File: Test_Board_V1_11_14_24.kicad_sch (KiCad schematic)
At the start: 9 parts, among them IC1 FE1.1S, J1 USB-A1HSW6, J2 USB-A1HSW6, J3 USB-A1HSW6

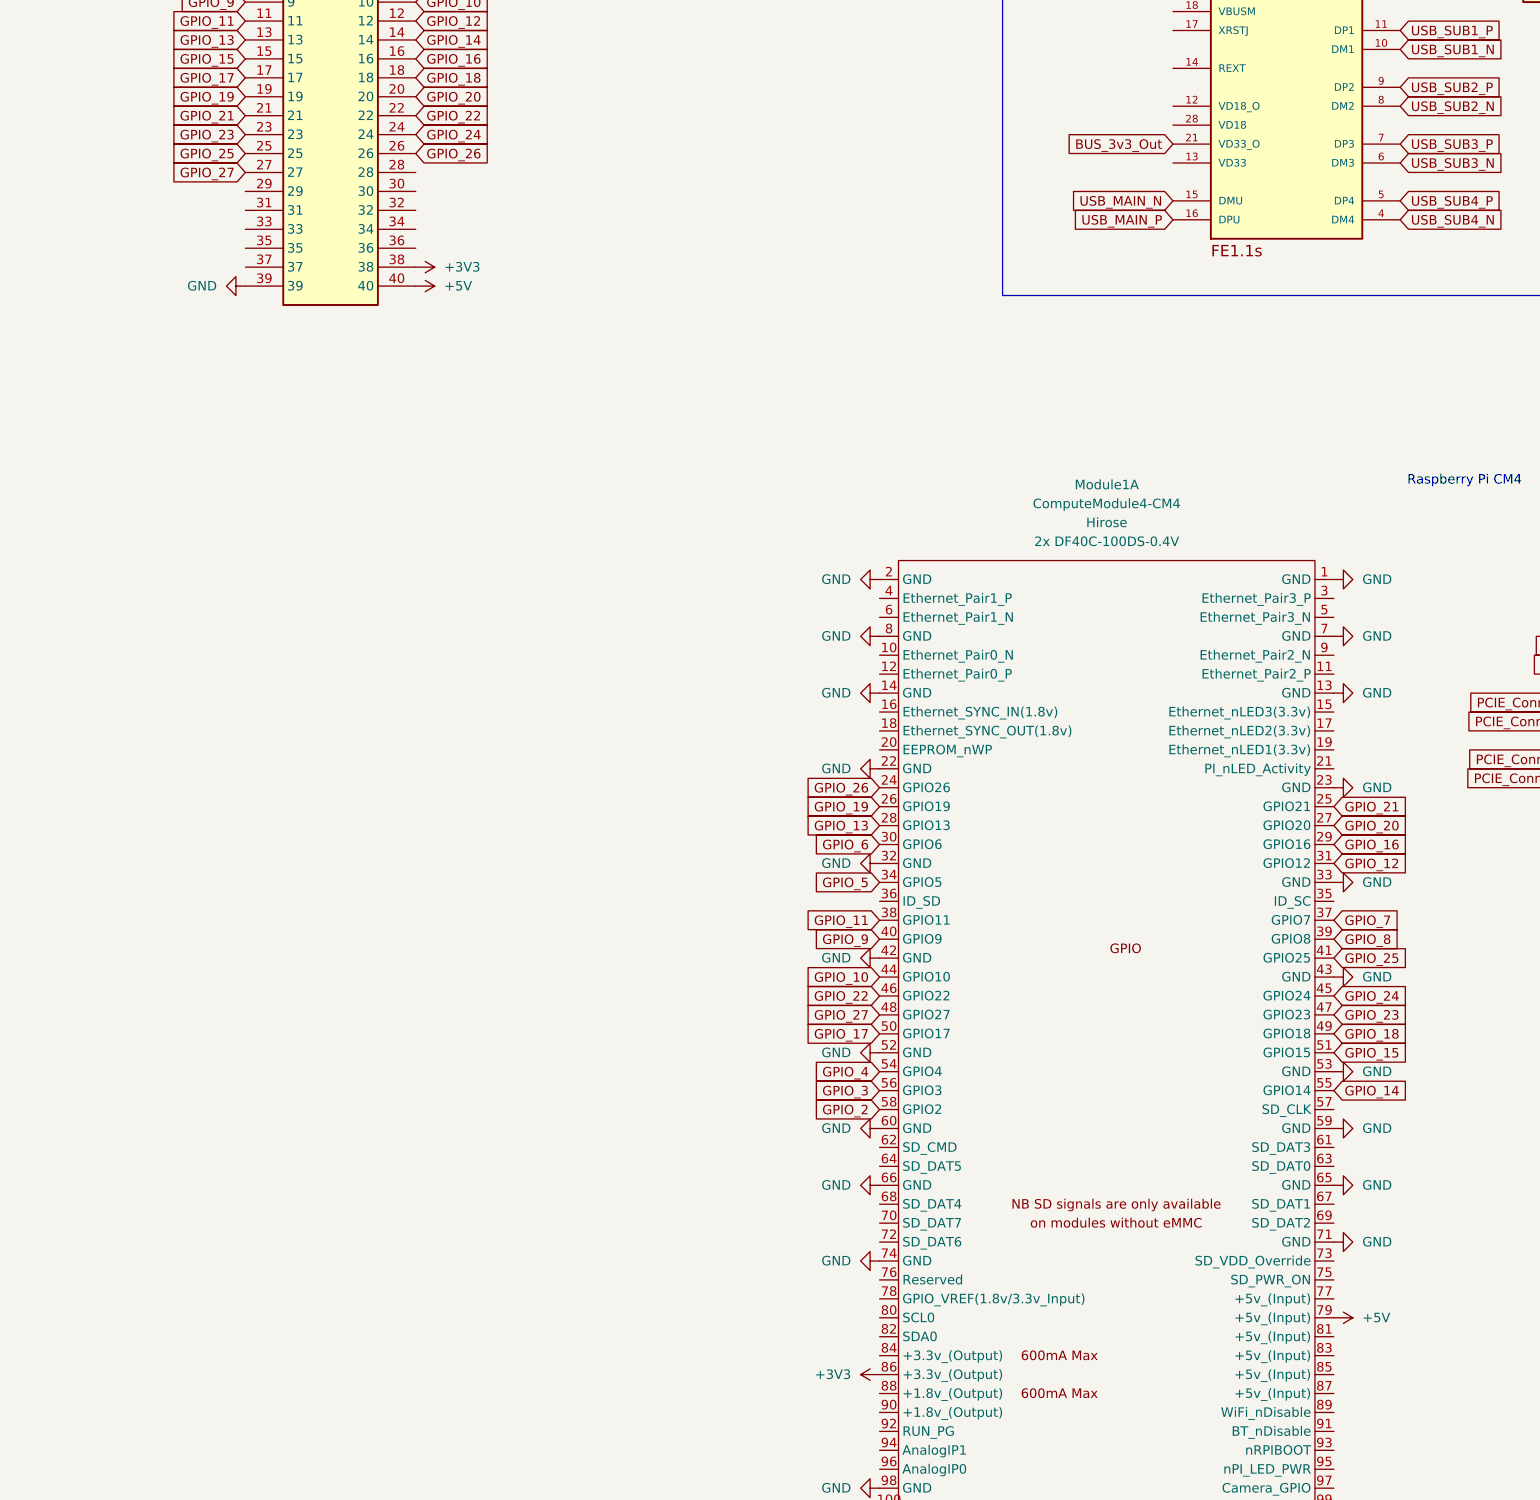
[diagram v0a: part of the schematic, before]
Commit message: footprints added and spaced
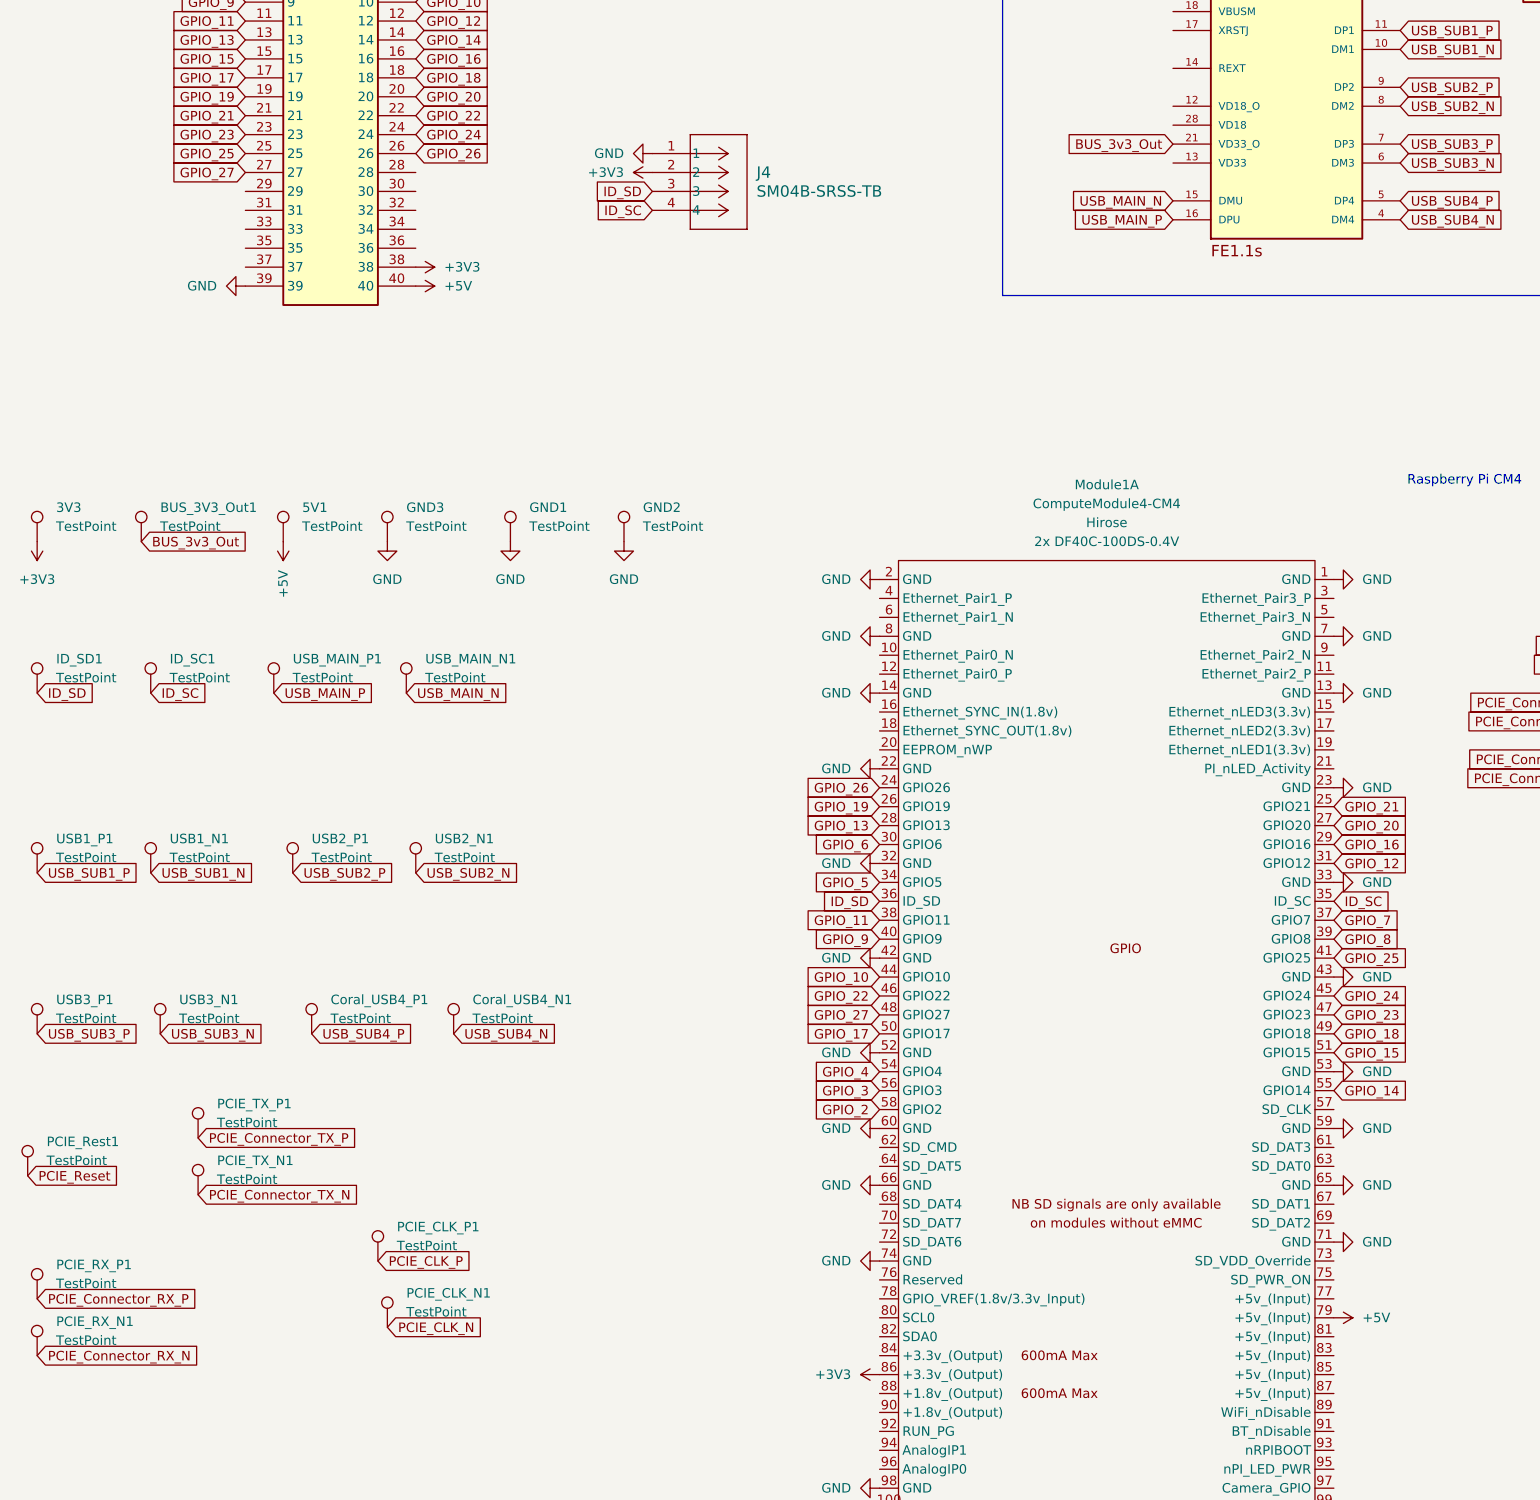
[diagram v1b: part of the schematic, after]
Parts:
- added 3V3, 5V1, BUS_3V3_Out1, Coral_USB4_N1, Coral_USB4_P1, GND1, GND2, GND3, ID_SC1, ID_SD1, PCIE_CLK_N1, PCIE_CLK_P1, PCIE_RX_N1, PCIE_RX_P1, PCIE_Rest1, PCIE_TX_N1, PCIE_TX_P1, USB1_N1, USB1_P1, USB2_N1, USB2_P1, USB3_N1, USB3_P1, USB_MAIN_N1, USB_MAIN_P1: TestPoint, TestPoint:TestPoint_Loop_D1.80mm_Drill1.0mm_Beaded, symbol Connector:TestPoint
- added J4: SM04B-SRSS-TB, SeniorDesign_Qwiic_Flat:CONN_SM04B-SRSS-TB_JST, symbol SeniorDesign_Qwiic_Flat:SM04B-SRSS-TB
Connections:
- net +3V3: now also 3V3.1, J4.2
- net +5V: now also 5V1.1
- net BUS_3v3_Out: now also BUS_3V3_Out1.1
- net GND: now also GND1.1, GND2.1, GND3.1, J4.1
- net PCIE_CLK_N: now also PCIE_CLK_N1.1
- net PCIE_CLK_P: now also PCIE_CLK_P1.1
- net PCIE_Connector_RX_N: now also PCIE_RX_N1.1
- net PCIE_Connector_RX_P: now also PCIE_RX_P1.1
- net PCIE_Connector_TX_N: now also PCIE_TX_N1.1
- net PCIE_Connector_TX_P: now also PCIE_TX_P1.1
- net PCIE_Reset: now also PCIE_Rest1.1
- net USB_MAIN_N: now also USB_MAIN_N1.1
- net USB_MAIN_P: now also USB_MAIN_P1.1
- net USB_SUB1_N: now also USB1_N1.1
- net USB_SUB1_P: now also USB1_P1.1
- net USB_SUB2_N: now also USB2_N1.1
- net USB_SUB2_P: now also USB2_P1.1
- net USB_SUB3_N: now also USB3_N1.1
- net USB_SUB3_P: now also USB3_P1.1
- net USB_SUB4_N: now also Coral_USB4_N1.1
- net USB_SUB4_P: now also Coral_USB4_P1.1
- net ID_SC: now reaches Module1.35 (ID_SC)
- net ID_SC: now also ID_SC1.1, J4.4
- net ID_SD: now reaches Module1.36 (ID_SD)
- net ID_SD: now also ID_SD1.1, J4.3

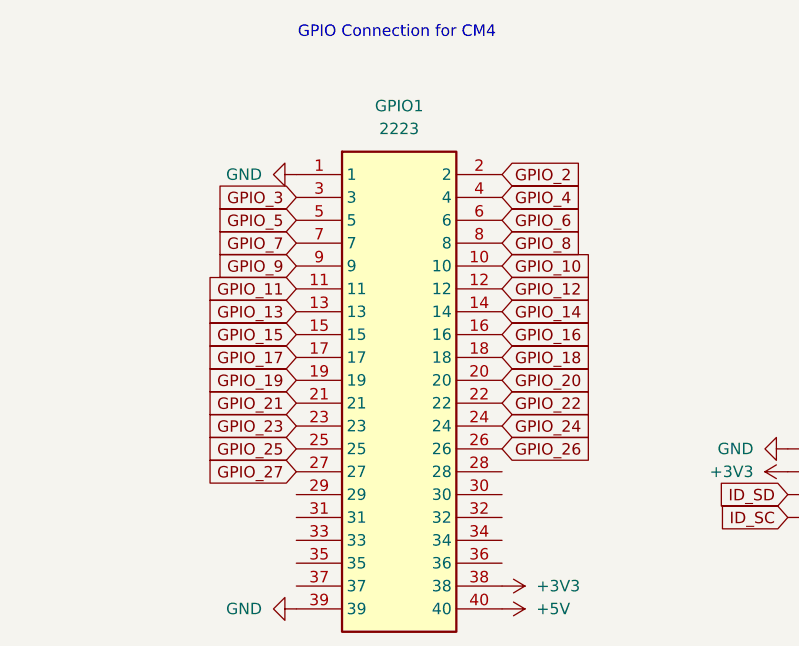
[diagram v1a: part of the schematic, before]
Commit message: All traces done except GPIO
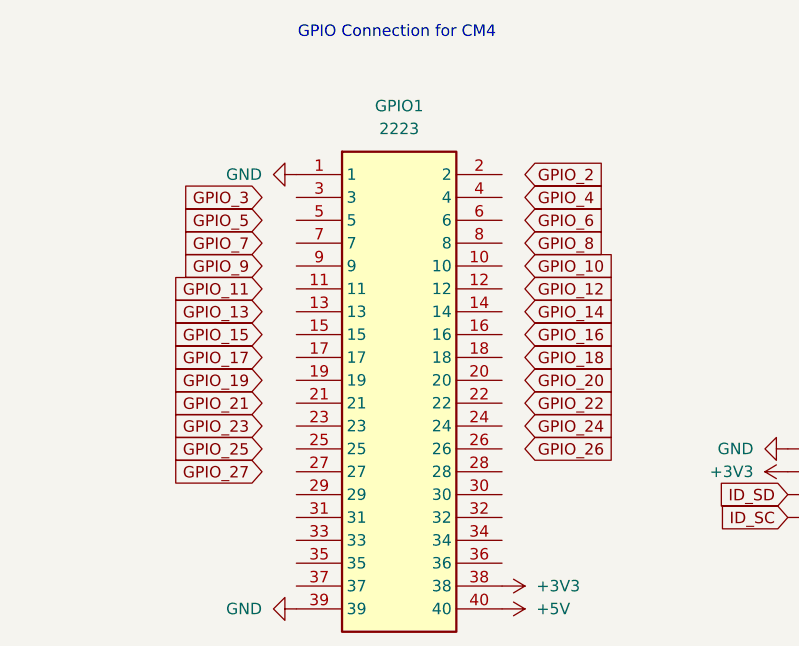
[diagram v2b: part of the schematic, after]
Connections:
- net GPIO_10: no longer GPIO1.10
- net GPIO_11: no longer GPIO1.11
- net GPIO_12: no longer GPIO1.12
- net GPIO_13: no longer GPIO1.13
- net GPIO_14: no longer GPIO1.14
- net GPIO_15: no longer GPIO1.15
- net GPIO_16: no longer GPIO1.16
- net GPIO_17: no longer GPIO1.17
- net GPIO_18: no longer GPIO1.18
- net GPIO_19: no longer GPIO1.19
- net GPIO_2: no longer GPIO1.2
- net GPIO_20: no longer GPIO1.20
- net GPIO_21: no longer GPIO1.21
- net GPIO_22: no longer GPIO1.22
- net GPIO_23: no longer GPIO1.23
- net GPIO_24: no longer GPIO1.24
- net GPIO_25: no longer GPIO1.25
- net GPIO_26: no longer GPIO1.26
- net GPIO_27: no longer GPIO1.27
- net GPIO_3: no longer GPIO1.3
- net GPIO_4: no longer GPIO1.4
- net GPIO_5: no longer GPIO1.5
- net GPIO_6: no longer GPIO1.6
- net GPIO_7: no longer GPIO1.7
- net GPIO_8: no longer GPIO1.8
- net GPIO_9: no longer GPIO1.9

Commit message: pcie connector fixed
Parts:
- added IC2: USB4715T-I_Y9X, QFN50P700X700X100-49N-D, symbol USB4715T-I_Y9X:USB4715T-I_Y9X
- PCIE1: footprint SeniorDesign_PCIEConnector:AMPHENOL_10082378-11100TLF -> 10018783-11110TLF:AMPHENOL_10018783-11110TLF
- renumbered BUS_3V3_Out1 to 3V3_Out1
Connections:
- net +5V: now also J1.1 (VBUS), J2.1 (VBUS), J3.1 (VBUS)
- net BUS_3v3_Out: no longer J1.1 (VBUS), J2.1 (VBUS), J3.1 (VBUS)
- net GND: now also IC2.49 (VSS); no longer IC1.1 (VSS)
- net USB_SUB1_N: now also IC1.11 (DP1), IC2.5 (FLEX_USB_DM1/PRT_DIS_M1); no longer IC1.10 (DM1)
- net USB_SUB1_P: now also IC1.10 (DM1), IC2.4 (FLEX_USB_DP1/PRT_DIS_P1); no longer IC1.11 (DP1)
- net USB_SUB2_N: now also IC1.9 (DP2), IC2.7 (FLEX_USB_DM2/PRT_DIS_M2); no longer IC1.8 (DM2)
- net USB_SUB2_P: now also IC1.8 (DM2), IC2.6 (FLEX_USB_DP2/PRT_DIS_P2); no longer IC1.9 (DP2)
- net USB_SUB3_N: now also IC1.7 (DP3), IC2.41 (FLEX_USB_DM3/PRT_DIS_M3); no longer IC1.6 (DM3)
- net USB_SUB3_P: now also IC1.6 (DM3), IC2.40 (FLEX_USB_DP3/PRT_DIS_P3); no longer IC1.7 (DP3)
- net USB_SUB4_N: now also IC1.5 (DP4), IC2.9 (FLEX_USB_DM4/PRT_DIS_M4); no longer IC1.4 (DM4)
- net USB_SUB4_P: now also IC1.4 (DM4), IC2.8 (FLEX_USB_DP4/PRT_DIS_P4); no longer IC1.5 (DP4)
- new net +3.3V: IC2.12 (VDDIO33_1), IC2.20 (VDDIO33_2), IC2.25 (VDDIO33_3), IC2.31 (VDDIO33_4), IC2.36 (VDDIO33_5), IC2.39 (VDDIO33_6)
- new net 1.2V_OUT: IC2.19 (VDDCR12)
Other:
- moved on the sheet: PCIE1
